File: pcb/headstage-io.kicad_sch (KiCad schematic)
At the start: 4 parts, among them J1 BSE-040-01-X-D-A

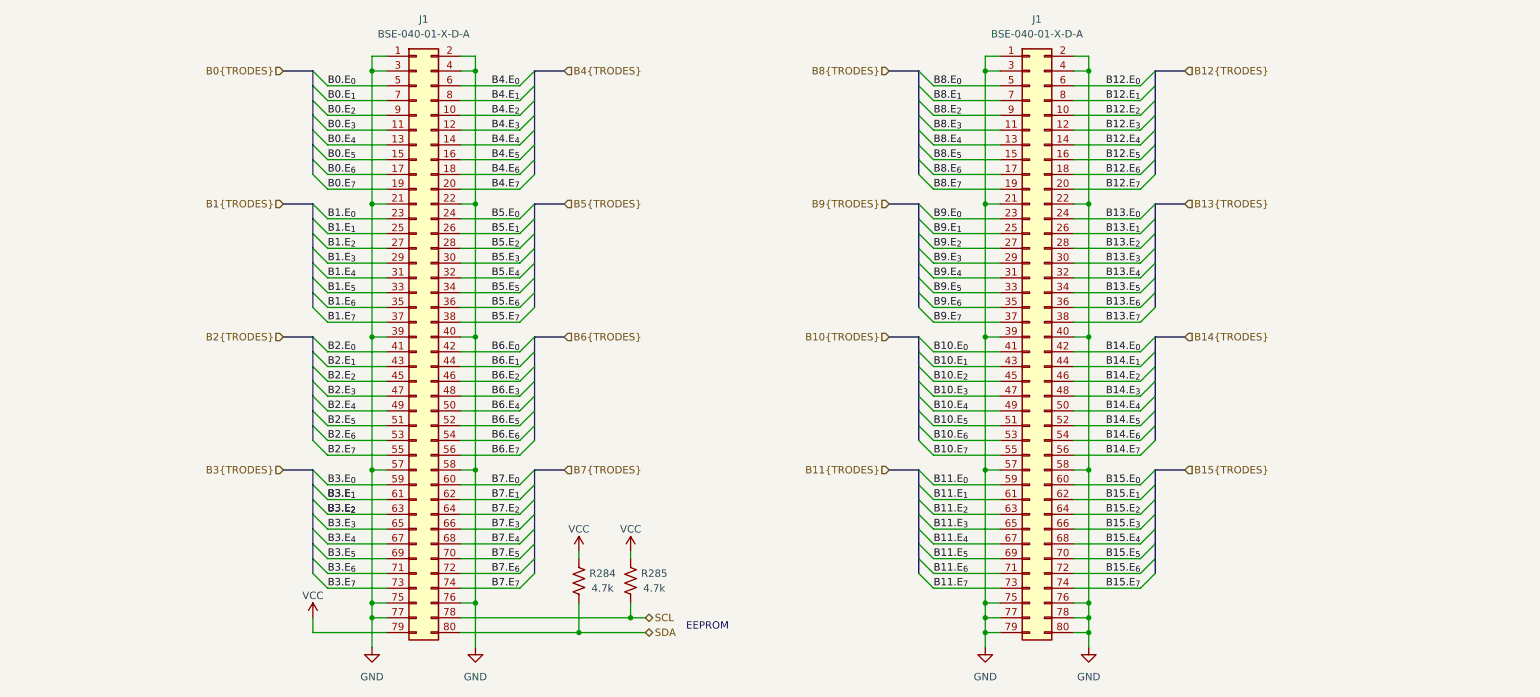
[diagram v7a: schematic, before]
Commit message: Start routing rev. A
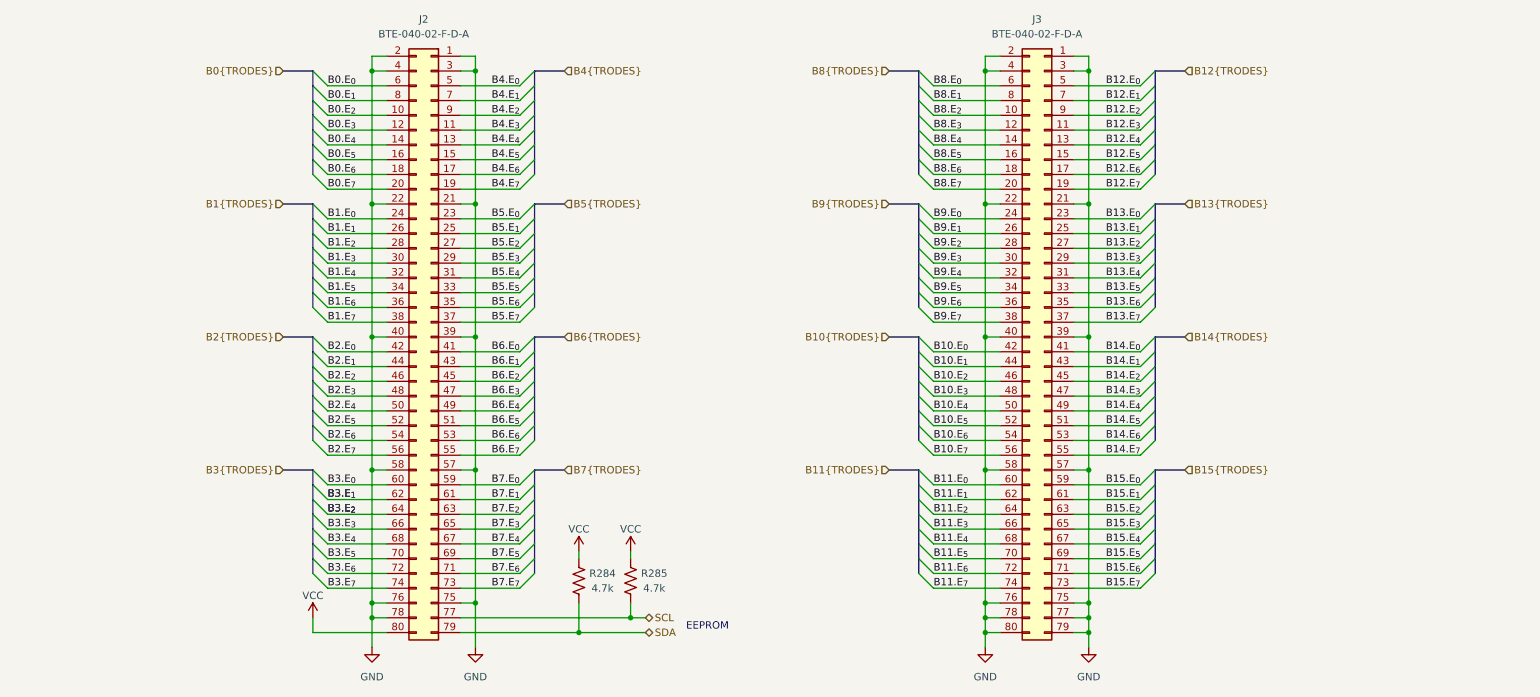
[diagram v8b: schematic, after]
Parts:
- removed J1 (x2): BSE-040-01-X-D-A, jonnew:SAMTEC_BSE-040-01-X-D-A, symbol Connector_Generic:Conn_02x40_Odd_Even
- added J2, J3: BTE-040-02-F-D-A, jonnew:SAMTEC_BTE-040-0x-L-D-A-K-TR, symbol Connector_Generic:Conn_02x40_Odd_Even
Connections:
- net B0.E_{0}: now also J2.6 (Pin_6)
- net B0.E_{1}: now also J2.8 (Pin_8)
- net B0.E_{2}: now also J2.10 (Pin_10)
- net B0.E_{3}: now also J2.12 (Pin_12)
- net B0.E_{4}: now also J2.14 (Pin_14)
- net B0.E_{5}: now also J2.16 (Pin_16)
- net B0.E_{6}: now also J2.18 (Pin_18)
- net B0.E_{7}: now also J2.20 (Pin_20)
- net B1.E_{0}: now also J2.24 (Pin_24)
- net B1.E_{1}: now also J2.26 (Pin_26)
- net B1.E_{2}: now also J2.28 (Pin_28)
- net B1.E_{3}: now also J2.30 (Pin_30)
- net B1.E_{4}: now also J2.32 (Pin_32)
- net B1.E_{5}: now also J2.34 (Pin_34)
- net B1.E_{6}: now also J2.36 (Pin_36)
- net B1.E_{7}: now also J2.38 (Pin_38)
- net B10.E_{0}: now also J3.42 (Pin_42)
- net B10.E_{1}: now also J3.44 (Pin_44)
- net B10.E_{2}: now also J3.46 (Pin_46)
- net B10.E_{3}: now also J3.48 (Pin_48)
- net B10.E_{4}: now also J3.50 (Pin_50)
- net B10.E_{5}: now also J3.52 (Pin_52)
- net B10.E_{6}: now also J3.54 (Pin_54)
- net B10.E_{7}: now also J3.56 (Pin_56)
- net B11.E_{0}: now also J3.60 (Pin_60)
- net B11.E_{1}: now also J3.62 (Pin_62)
- net B11.E_{2}: now also J3.64 (Pin_64)
- net B11.E_{3}: now also J3.66 (Pin_66)
- net B11.E_{4}: now also J3.68 (Pin_68)
- net B11.E_{5}: now also J3.70 (Pin_70)
- net B11.E_{6}: now also J3.72 (Pin_72)
- net B11.E_{7}: now also J3.74 (Pin_74)
- net B12.E_{0}: now also J3.5 (Pin_5)
- net B12.E_{1}: now also J3.7 (Pin_7)
- net B12.E_{2}: now also J3.9 (Pin_9)
- net B12.E_{3}: now also J3.11 (Pin_11)
- net B12.E_{4}: now also J3.13 (Pin_13)
- net B12.E_{5}: now also J3.15 (Pin_15)
- net B12.E_{6}: now also J3.17 (Pin_17)
- net B12.E_{7}: now also J3.19 (Pin_19)
- net B13.E_{0}: now also J3.23 (Pin_23)
- net B13.E_{1}: now also J3.25 (Pin_25)
- net B13.E_{2}: now also J3.27 (Pin_27)
- net B13.E_{3}: now also J3.29 (Pin_29)
- net B13.E_{4}: now also J3.31 (Pin_31)
- net B13.E_{5}: now also J3.33 (Pin_33)
- net B13.E_{6}: now also J3.35 (Pin_35)
- net B13.E_{7}: now also J3.37 (Pin_37)
- net B14.E_{0}: now also J3.41 (Pin_41)
- net B14.E_{1}: now also J3.43 (Pin_43)
- net B14.E_{2}: now also J3.45 (Pin_45)
- net B14.E_{3}: now also J3.47 (Pin_47)
- net B14.E_{4}: now also J3.49 (Pin_49)
- net B14.E_{5}: now also J3.51 (Pin_51)
- net B14.E_{6}: now also J3.53 (Pin_53)
- net B14.E_{7}: now also J3.55 (Pin_55)
- net B15.E_{0}: now also J3.59 (Pin_59)
- net B15.E_{1}: now also J3.61 (Pin_61)
- net B15.E_{2}: now also J3.63 (Pin_63)
- net B15.E_{3}: now also J3.65 (Pin_65)
- net B15.E_{4}: now also J3.67 (Pin_67)
- net B15.E_{5}: now also J3.69 (Pin_69)
- net B15.E_{6}: now also J3.71 (Pin_71)
- net B15.E_{7}: now also J3.73 (Pin_73)
- net B2.E_{0}: now also J2.42 (Pin_42)
- net B2.E_{1}: now also J2.44 (Pin_44)
- net B2.E_{2}: now also J2.46 (Pin_46)
- net B2.E_{3}: now also J2.48 (Pin_48)
- net B2.E_{4}: now also J2.50 (Pin_50)
- net B2.E_{5}: now also J2.52 (Pin_52)
- net B2.E_{6}: now also J2.54 (Pin_54)
- net B2.E_{7}: now also J2.56 (Pin_56)
- net B3.E_{0}: now also J2.60 (Pin_60)
- net B3.E_{1}: now also J2.62 (Pin_62)
- net B3.E_{2}: now also J2.64 (Pin_64)
- net B3.E_{3}: now also J2.66 (Pin_66)
- net B3.E_{4}: now also J2.68 (Pin_68)
- net B3.E_{5}: now also J2.70 (Pin_70)
- net B3.E_{6}: now also J2.72 (Pin_72)
- net B3.E_{7}: now also J2.74 (Pin_74)
- net B4.E_{0}: now also J2.5 (Pin_5)
- net B4.E_{1}: now also J2.7 (Pin_7)
- net B4.E_{2}: now also J2.9 (Pin_9)
- net B4.E_{3}: now also J2.11 (Pin_11)
- net B4.E_{4}: now also J2.13 (Pin_13)
- net B4.E_{5}: now also J2.15 (Pin_15)
- net B4.E_{6}: now also J2.17 (Pin_17)
- net B4.E_{7}: now also J2.19 (Pin_19)
- net B5.E_{0}: now also J2.23 (Pin_23)
- net B5.E_{1}: now also J2.25 (Pin_25)
- net B5.E_{2}: now also J2.27 (Pin_27)
- net B5.E_{3}: now also J2.29 (Pin_29)
- net B5.E_{4}: now also J2.31 (Pin_31)
- net B5.E_{5}: now also J2.33 (Pin_33)
- net B5.E_{6}: now also J2.35 (Pin_35)
- net B5.E_{7}: now also J2.37 (Pin_37)
- net B6.E_{0}: now also J2.41 (Pin_41)
- net B6.E_{1}: now also J2.43 (Pin_43)
- net B6.E_{2}: now also J2.45 (Pin_45)
- net B6.E_{3}: now also J2.47 (Pin_47)
- net B6.E_{4}: now also J2.49 (Pin_49)
- net B6.E_{5}: now also J2.51 (Pin_51)
- net B6.E_{6}: now also J2.53 (Pin_53)
- net B6.E_{7}: now also J2.55 (Pin_55)
- net B7.E_{0}: now also J2.59 (Pin_59)
- net B7.E_{1}: now also J2.61 (Pin_61)
- net B7.E_{2}: now also J2.63 (Pin_63)
- net B7.E_{3}: now also J2.65 (Pin_65)
- net B7.E_{4}: now also J2.67 (Pin_67)
- net B7.E_{5}: now also J2.69 (Pin_69)
- net B7.E_{6}: now also J2.71 (Pin_71)
- net B7.E_{7}: now also J2.73 (Pin_73)
- net B8.E_{0}: now also J3.6 (Pin_6)
- net B8.E_{1}: now also J3.8 (Pin_8)
- net B8.E_{2}: now also J3.10 (Pin_10)
- net B8.E_{3}: now also J3.12 (Pin_12)
- net B8.E_{4}: now also J3.14 (Pin_14)
- net B8.E_{5}: now also J3.16 (Pin_16)
- net B8.E_{6}: now also J3.18 (Pin_18)
- net B8.E_{7}: now also J3.20 (Pin_20)
- net B9.E_{0}: now also J3.24 (Pin_24)
- net B9.E_{1}: now also J3.26 (Pin_26)
- net B9.E_{2}: now also J3.28 (Pin_28)
- net B9.E_{3}: now also J3.30 (Pin_30)
- net B9.E_{4}: now also J3.32 (Pin_32)
- net B9.E_{5}: now also J3.34 (Pin_34)
- net B9.E_{6}: now also J3.36 (Pin_36)
- net B9.E_{7}: now also J3.38 (Pin_38)
- net GND: now also J2.1 (Pin_1), J2.2 (Pin_2), J2.21 (Pin_21), J2.22 (Pin_22), J2.3 (Pin_3), J2.39 (Pin_39), J2.4 (Pin_4), J2.40 (Pin_40), J2.57 (Pin_57), J2.58 (Pin_58), J2.75 (Pin_75), J2.76 (Pin_76), J2.78 (Pin_78), J3.1 (Pin_1), J3.2 (Pin_2), J3.21 (Pin_21), J3.22 (Pin_22), J3.3 (Pin_3), J3.39 (Pin_39), J3.4 (Pin_4), J3.40 (Pin_40), J3.57 (Pin_57), J3.58 (Pin_58), J3.75 (Pin_75), J3.76 (Pin_76), J3.77 (Pin_77), J3.78 (Pin_78), J3.79 (Pin_79), J3.80 (Pin_80)
- net SCL: now also J2.77 (Pin_77)
- net SDA: now also J2.79 (Pin_79)
- net VCC: now also J2.80 (Pin_80)
